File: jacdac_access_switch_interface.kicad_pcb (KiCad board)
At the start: 2 copper layers, 25 x 35 mm, 26 parts, among them J1 Conn_Jacdac_CardEdge, J2 Conn_HackConnect, J3 jack_3.5_pj313d, J4 jack_3.5_pj313d, U1 NCP114ASN330T1G, U2 STM32G031J6M6, U3 AQY282, U4 AQY282

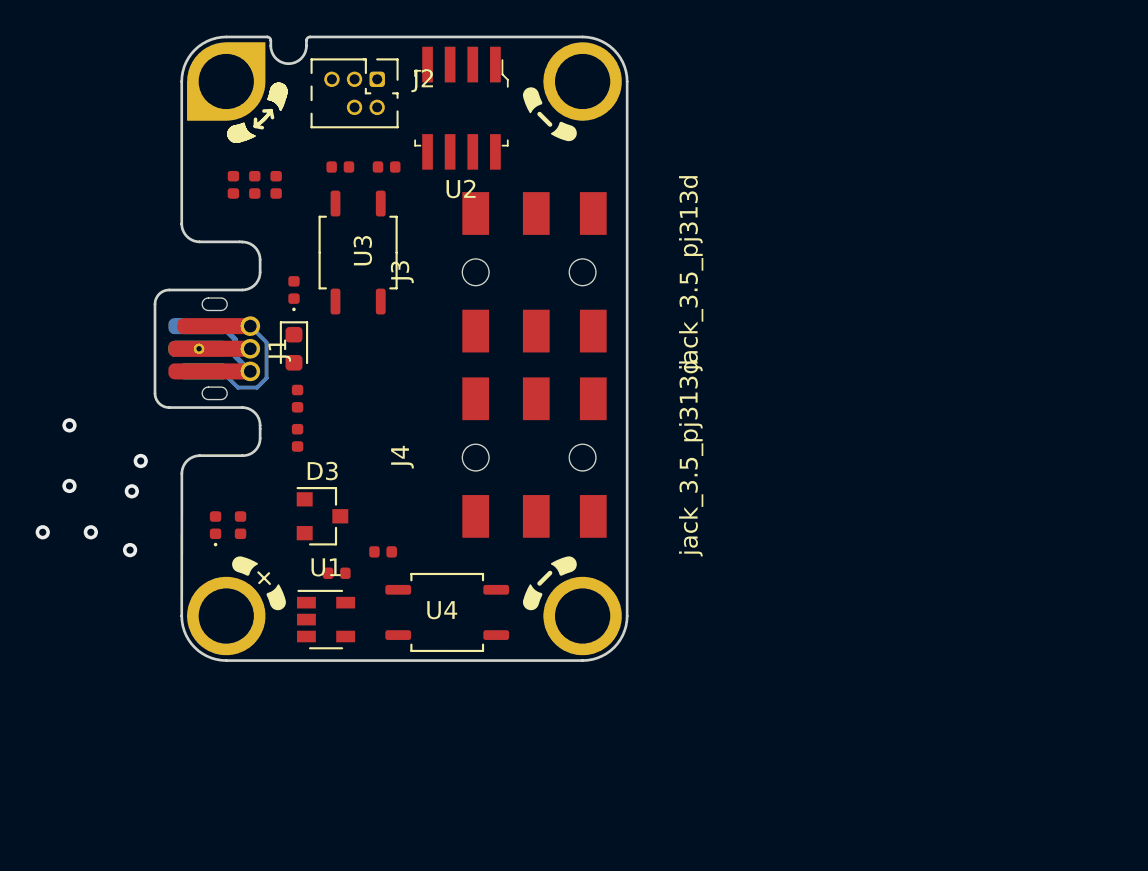
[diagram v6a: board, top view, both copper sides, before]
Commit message: Placing components for 30x20mm pcb
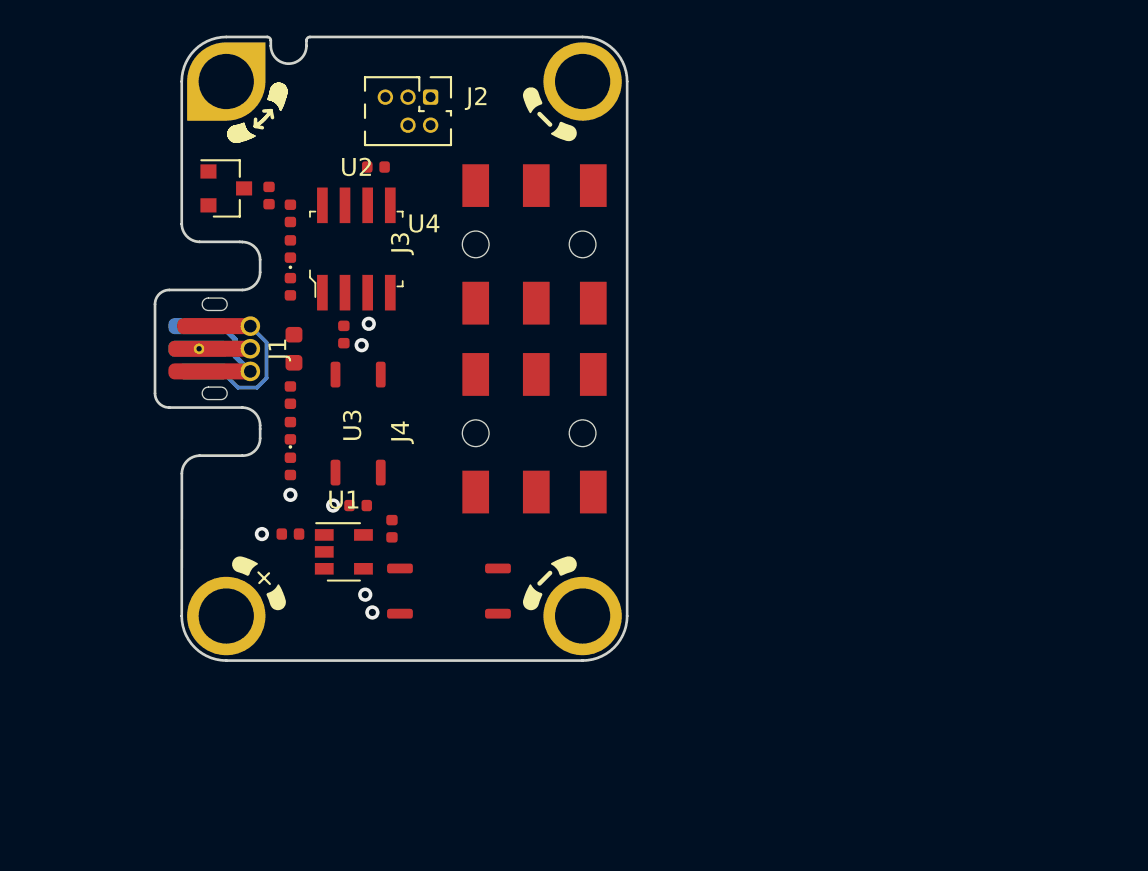
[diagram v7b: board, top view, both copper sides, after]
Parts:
- MH2: value Val** -> jacdac_hole_GND_MH2
- MH4: value Val** -> jacdac_hole_GND_MH4
- moved D3 19.2 mm to (150.0, 76.0)
- moved U2 9.86 mm to (157.3, 79.4), turned to 0 degrees
- moved C4 9.70 mm to (156.6, 84.2), turned to -90 degrees
- moved U3 9.60 mm to (157.4, 89.2), turned to 90 degrees
- moved D2 5.34 mm to (153.6, 91.6), turned to -90 degrees
- moved FB1 4.12 mm to (153.6, 79.4), turned to -90 degrees
- moved C2 3.98 mm to (157.4, 93.8)
- moved U1 3.93 mm to (156.6, 96.4)
- moved J2 3.16 mm to (161.5, 71.7)
- moved C1 2.84 mm to (153.6, 95.4), turned to 180 degrees
- moved R5 2.43 mm to (153.6, 87.6), turned to 90 degrees
- moved R1 2.09 mm to (152.4, 76.4), turned to -90 degrees
- moved R2 2.00 mm to (158.4, 74.8)
- moved R4 1.84 mm to (153.6, 89.6), turned to -90 degrees
- moved C3 1.79 mm to (153.6, 77.4)
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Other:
- board text added: "Switch output v1.4"
- board text removed: "Switch output v1.3"

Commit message: Components placed, ready for routing
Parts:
- moved R1 1.63 mm to (153.6, 75.3)
- moved D3 1.24 mm to (151.2, 75.7)
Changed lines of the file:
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@@
   )
   (footprint "jacdac_access_switch_interface:R_0402_1005Metric" (layer "F.Cu")
-    (at 152.4 76.4 -90)
+    (at 153.6 75.3 -90)
     (descr "Resistor SMD 0402 (1005 Metric), square (rectangular) end terminal, IPC_7351 nominal, (Body size source: http://www.tortai-tech.com/upload/download/2011102023233369053.pdf), generated with kicad-footprint-generator")
     (tags "resistor")
@@
   )
   (footprint "jacdac_access_switch_interface:SOT-23" (layer "F.Cu")
-    (at 150 76)
+    (at 151.2 75.7)
     (descr "SOT-23, Standard")
     (tags "SOT-23")
